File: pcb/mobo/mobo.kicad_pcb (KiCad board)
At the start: 2 copper layers, 51.6 x 89 mm, 72 parts, among them J1 SWD_10, J2 PEEL_MOTOR, J3 DRIVE_MOTOR, J4 SW1, J5 SPRING_FINGERS, J6 SW2, J7 SW1, J8 USART1, J9 SWD_10, U1 STM32F031C6Tx, U2 STM32F031K6Ux, U4 AP1117-33, U5 MC34063AD, U6 MAX3078E, U7 DRV8837, U8 DRV8837, Y1 8MHz

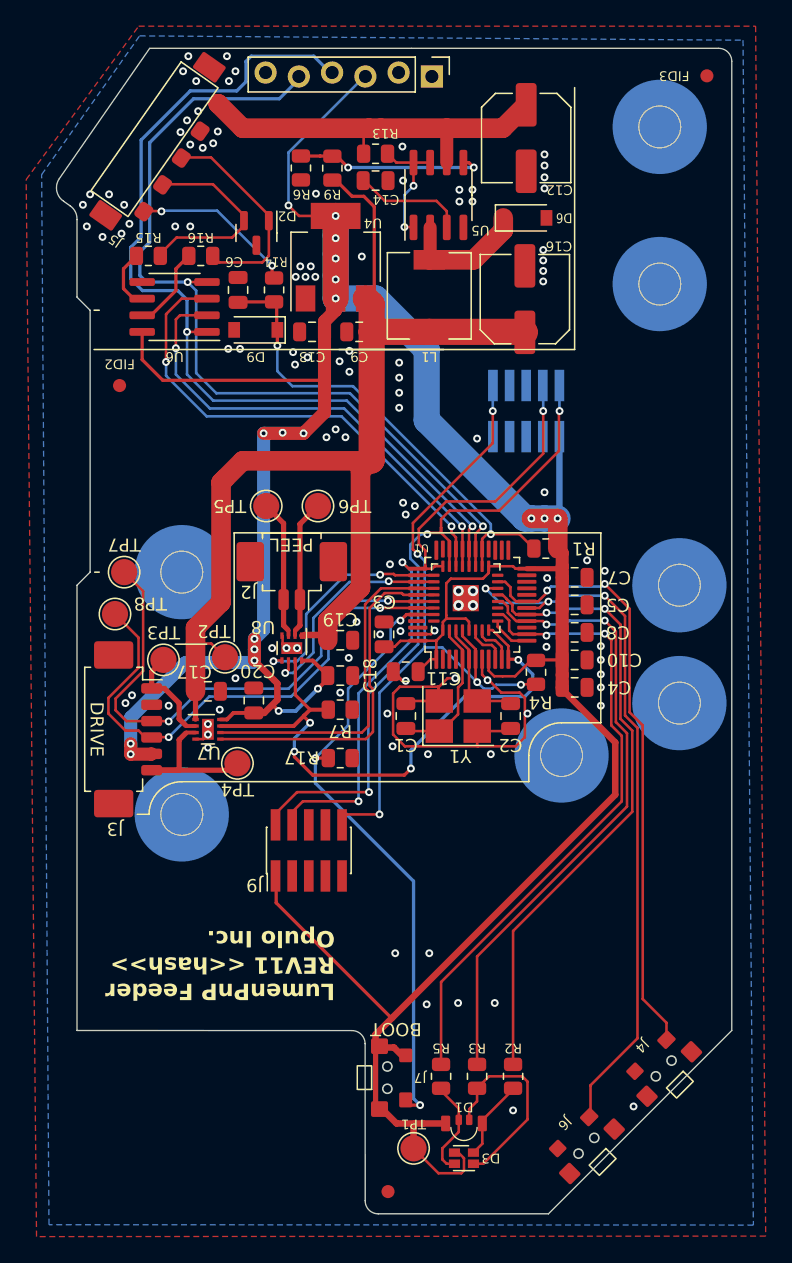
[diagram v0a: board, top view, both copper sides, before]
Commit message: tidy pcb. 3dprinted jigs.
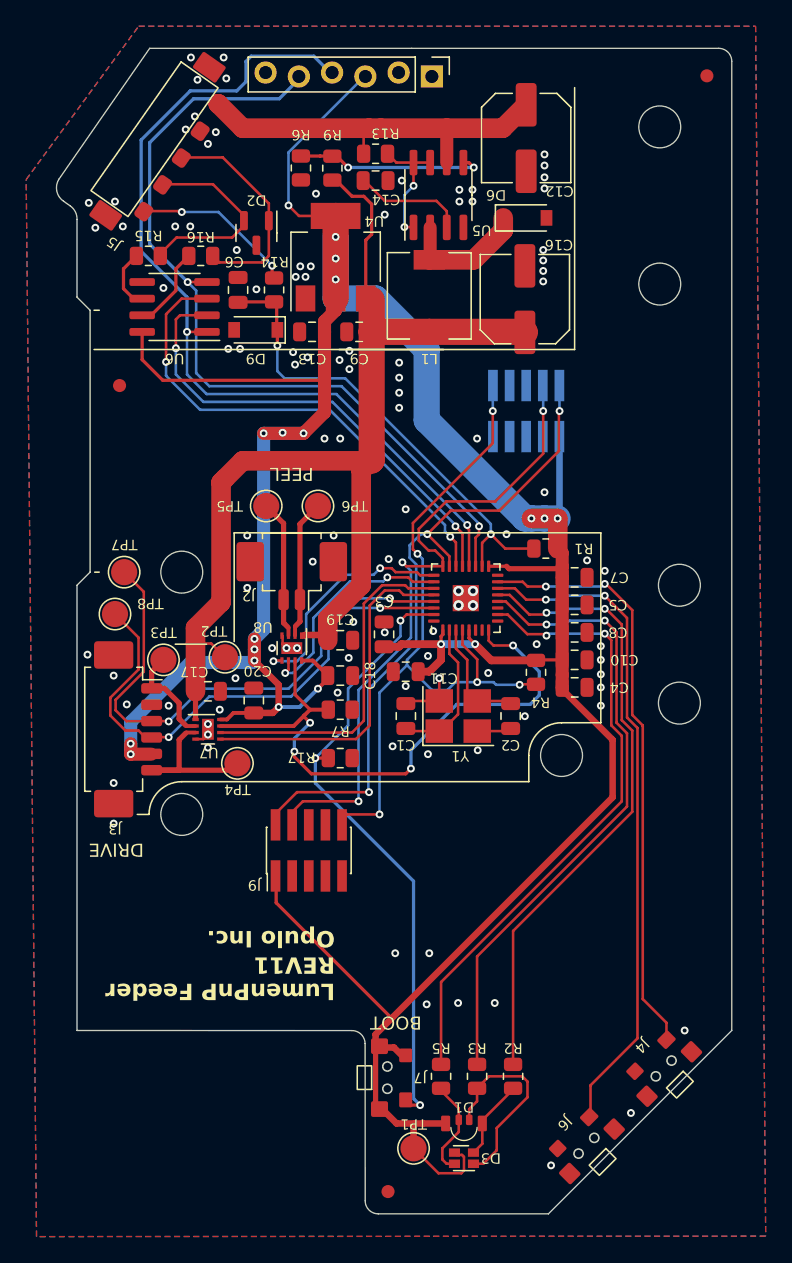
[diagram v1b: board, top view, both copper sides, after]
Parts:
- removed the G*** at (122.0, 79.1)
- removed U1: STM32F031C6Tx, Package_QFP:LQFP-48_7x7mm_P0.5mm
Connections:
- J2 pad MP: (no net) -> GND
- J3 pad MP: (no net) -> GND
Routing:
- net GND: track 39.6 -> 8.96 mm, vias 110 -> 106
- net +3V3: track 269.4 -> 260.8 mm
- net SW2: track 55.1 -> 51.2 mm, vias 3 -> 2
- net PA1: track 3.26 -> 0.00 mm
- net PA0: track 3.24 -> 0.00 mm
- net PA3: track 3.10 -> 0.00 mm
- net MCU_TX: track 66.7 -> 64.0 mm
- net MCU_RX: track 71.5 -> 69.0 mm
- net SW1: track 46.6 -> 45.2 mm
- net MOTOR_ENABLE: track 47.2 -> 48.4 mm
- net RESET: track 54.9 -> 55.8 mm
- net SWDIO: track 52.5 -> 51.8 mm
- net +10V: track 86.7 -> 86.0 mm
- net PEEL1: track 16.8 -> 17.3 mm
- net RS-485-: track 16.4 -> 16.9 mm
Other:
- board text added: "LumenPnP Feeder REV11 Opulo Inc."
- board text removed: "LumenPnP Feeder REV11 <<hash>> Opulo Inc."
